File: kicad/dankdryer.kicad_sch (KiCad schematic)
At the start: 25 parts, among them J1 Barreljack, J4 heater, J5 Screw_Terminal_01x04, J7 5kg load cell, J8 motor, J9 Conn_01x04, U2 TPS62162DSG, U3 HT7550, U6 ESP32-C6-MINI-1U-H4

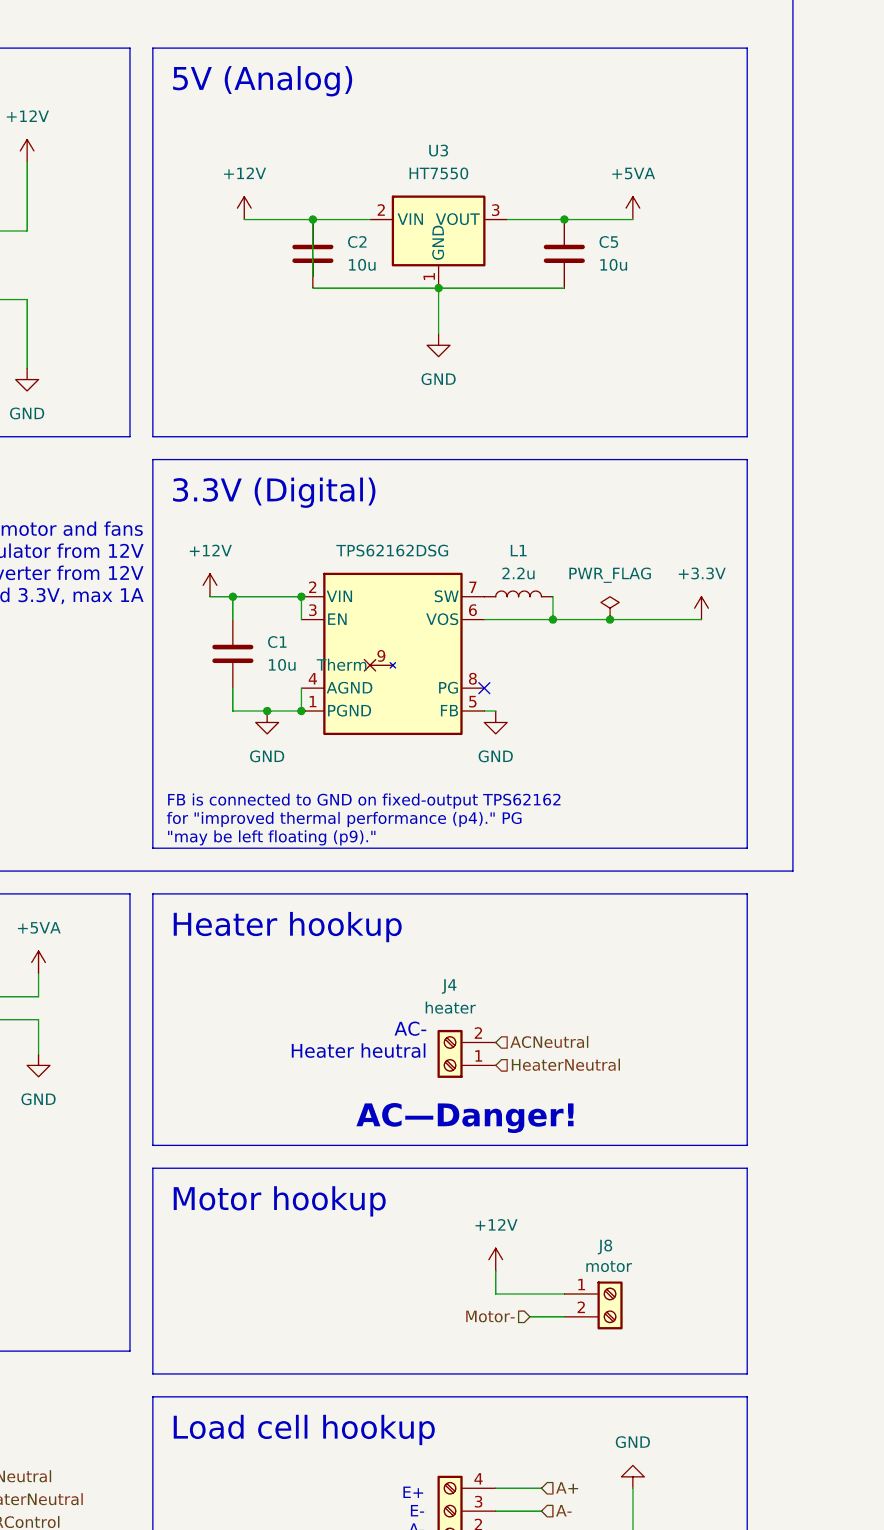
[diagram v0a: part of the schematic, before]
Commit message: kicad: note about AVDD on NAU7802
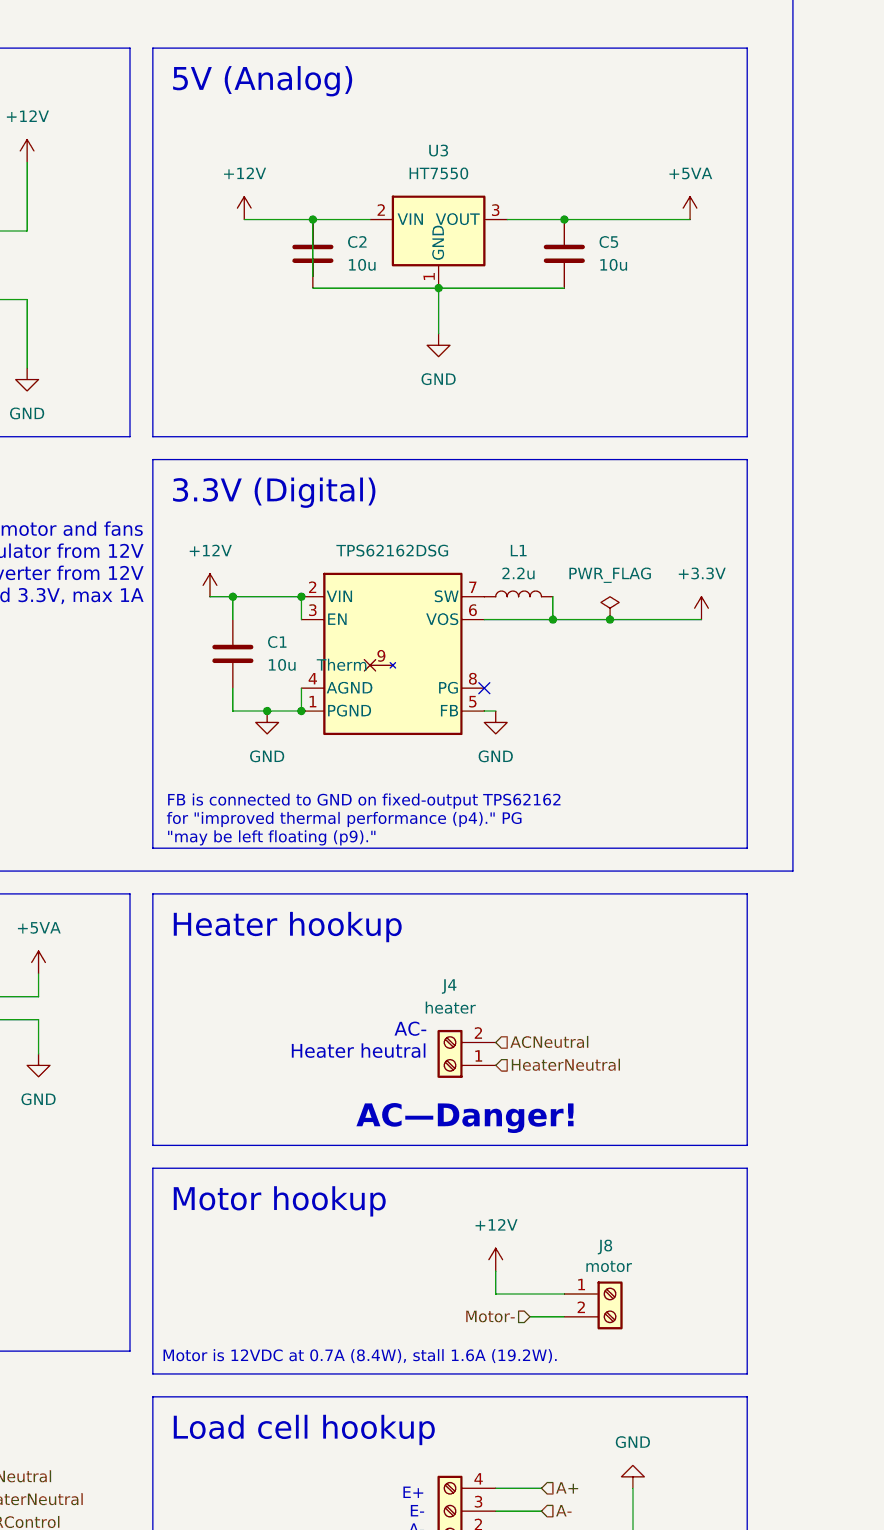
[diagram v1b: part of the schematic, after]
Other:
- note added: "Motor is 12VDC at 0.7A (8.4W), stall 1.6A (19.2W)."
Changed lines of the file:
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@@
 	(wire
 		(pts
-			(xy 134.62 41.91) (xy 142.24 41.91)
+			(xy 134.62 41.91) (xy 148.59 41.91)
 		)
 		(stroke
@@
 		(exclude_from_sim no)
 		(at 21.336 164.084 0)
+		(effects
+			(font
+				(size 1.27 1.27)
+			)
+			(justify left)
+		)
+	)
+	(text "Motor is 12VDC at 0.7A (8.4W), stall 1.6A (19.2W)."
+		(exclude_from_sim no)
+		(at 89.916 168.402 0)
 		(effects
 			(font
@@
 	(symbol
 		(lib_id "power:+5VA")
-		(at 142.24 41.91 0)
+		(at 148.59 41.91 0)
 		(unit 1)
 		(exclude_from_sim no)
@@
 		(fields_autoplaced yes)
 		(property "Reference" "#PWR015"
-			(at 142.24 45.72 0)
+			(at 148.59 45.72 0)
 			(effects
 				(font
@@
 		)
 		(property "Value" "+5VA"
-			(at 142.24 36.83 0)
+			(at 148.59 36.83 0)
 			(effects
 				(font
@@
 		)
 		(property "Footprint" ""
-			(at 142.24 41.91 0)
+			(at 148.59 41.91 0)
 			(effects
 				(font
@@
 		)
 		(property "Datasheet" ""
-			(at 142.24 41.91 0)
+			(at 148.59 41.91 0)
 			(effects
 				(font
@@
 		)
 		(property "Description" "Power symbol creates a global label with name \"+5VA\""
-			(at 142.24 41.91 0)
+			(at 148.59 41.91 0)
 			(effects
 				(font

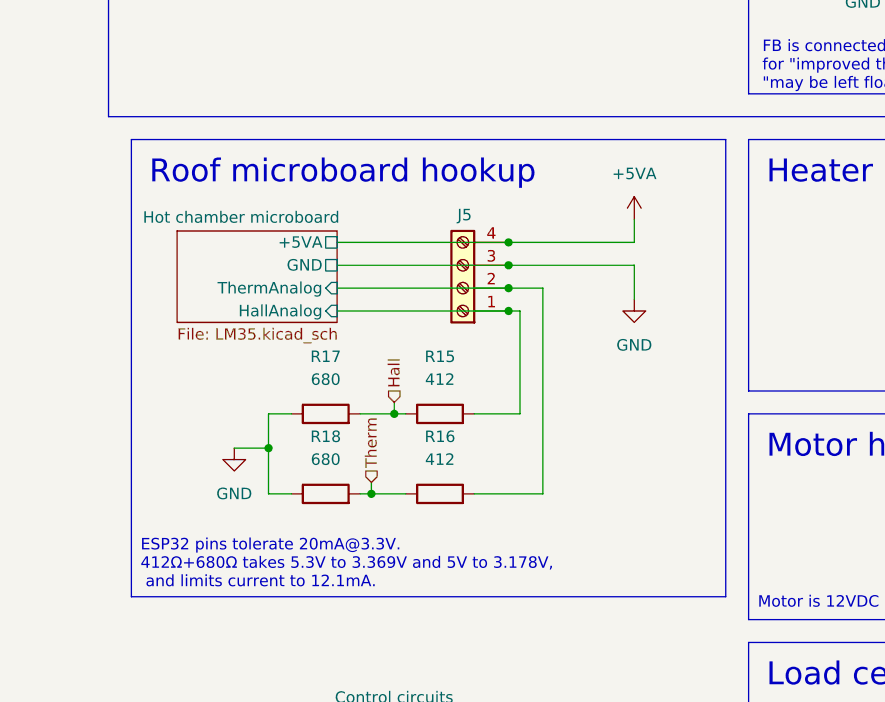
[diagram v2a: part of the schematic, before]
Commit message: take 3.3V to microboard rather than dividing 5V on return from hall sensor
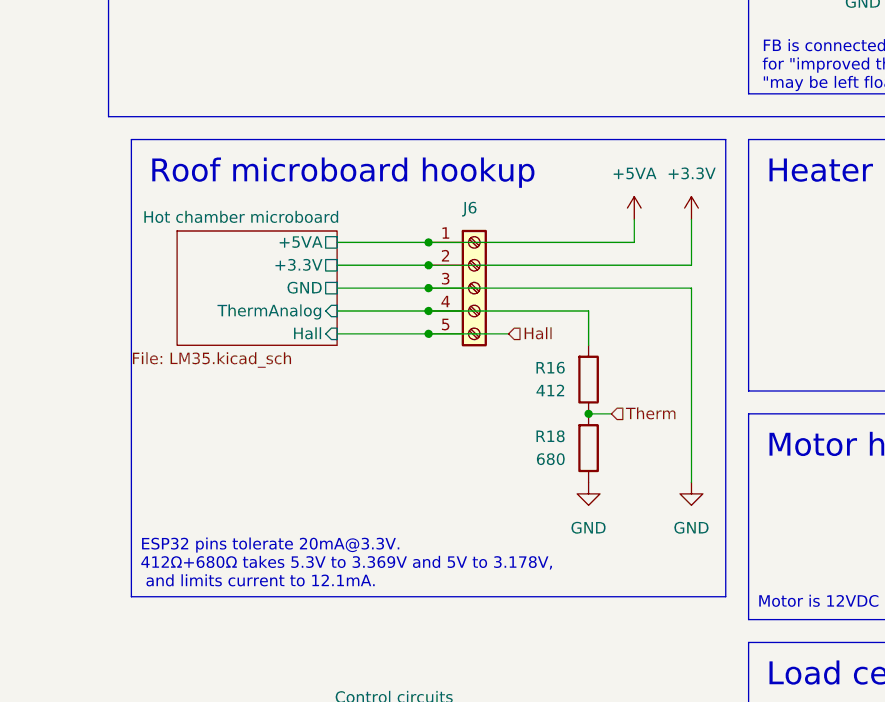
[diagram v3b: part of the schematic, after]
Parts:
- removed J5: Screw_Terminal_01x04, dank:TerminalBlock_bornier-4_P5.08mm, symbol Connector:Screw_Terminal_01x04
- removed R15: 412, PCM_Resistor_SMD_AKL:R_0805_2012Metric_Pad1.15x1.40mm_HandSolder, symbol Device:R
- removed R17: 680, PCM_Resistor_SMD_AKL:R_0805_2012Metric_Pad1.15x1.40mm_HandSolder, symbol Device:R
- added J6: Screw_Terminal_01x05, dank:TerminalBlock_bornier-5_P5.08mm, symbol Connector:Screw_Terminal_01x05
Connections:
- net +3.3V: now also J6.2 (Pin_2)
- net +5VA: now also J6.1 (Pin_1)
- net GND: now also J6.3 (Pin_3)
- net Hall: now also J6.5 (Pin_5)
- net Hot chamber microboard/ThermAnalog: now also J6.4 (Pin_4)
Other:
- sheet Hot chamber microboard ports: added +3.3V, Hall; removed HallAnalog
- moved on the sheet: R16, R18

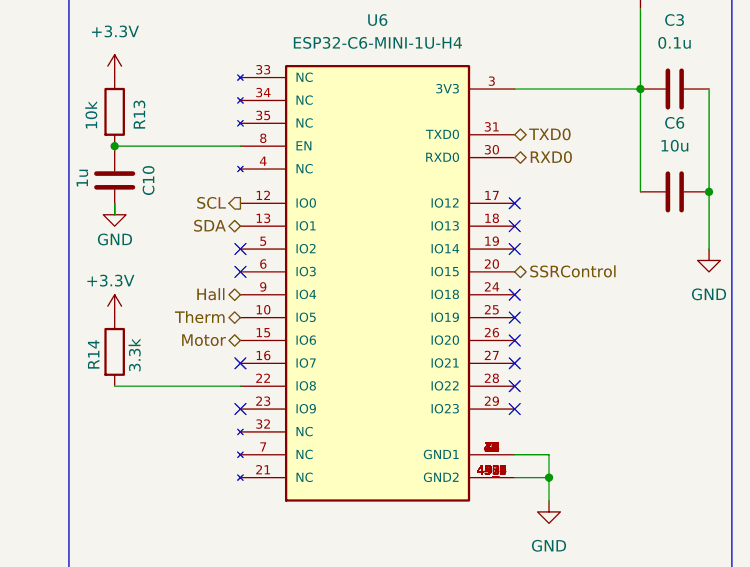
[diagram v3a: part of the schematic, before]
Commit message: get off the strapping pins. hardware version 1.0
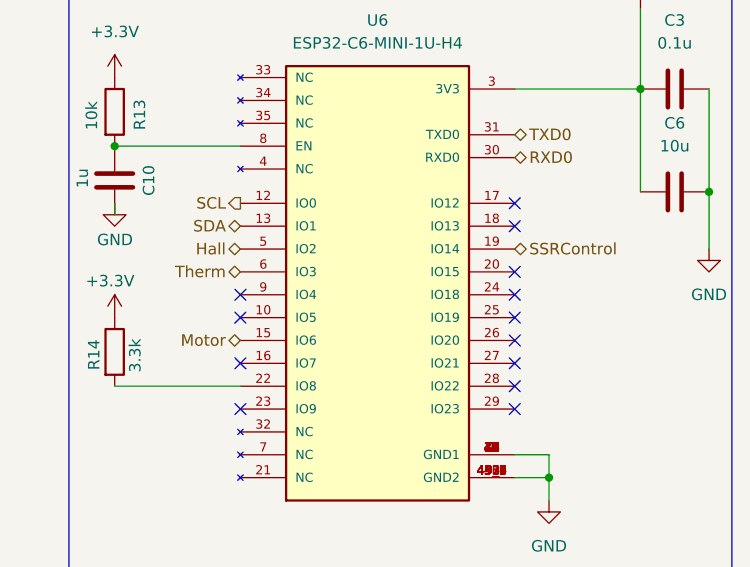
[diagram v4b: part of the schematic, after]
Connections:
- net Hall: now also U6.5 (IO2); no longer U6.9 (IO4)
- net SSRControl: now also U6.19 (IO14); no longer U6.20 (IO15)
- net Therm: now also U6.6 (IO3); no longer U6.10 (IO5)
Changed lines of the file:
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@@
 	(title_block
 		(title "Dankdryer")
-		(date "2024-12-26")
-		(rev "0.99")
+		(date "2024-12-31")
+		(rev "1.0")
 		(company "Dirty South Supercomputing")
 		(comment 1 "nick black")
@@
 	)
 	(no_connect
+		(at 189.23 69.85)
+	)
+	(no_connect
 		(at 219.71 57.15)
 	)
 	(no_connect
-		(at 189.23 62.23)
-	)
-	(no_connect
 		(at 219.71 77.47)
 	)
@@
 	)
 	(no_connect
-		(at 189.23 64.77)
-	)
-	(no_connect
 		(at 125.73 93.98)
 	)
 	(no_connect
-		(at 219.71 62.23)
+		(at 189.23 67.31)
 	)
 	(no_connect
 		(at 44.45 45.72)
+	)
+	(no_connect
+		(at 219.71 64.77)
 	)
 	(no_connect
@@
 	(hierarchical_label "Hall"
 		(shape bidirectional)
-		(at 189.23 67.31 180)
+		(at 189.23 62.23 180)
 		(fields_autoplaced yes)
 		(effects
@@
 			)
 			(justify right)
-		)
-	)
-	(hierarchical_label "SSRControl"
-		(shape bidirectional)
-		(at 219.71 64.77 0)
-		(fields_autoplaced yes)
-		(effects
-			(font
-				(size 1.27 1.27)
-			)
-			(justify left)
 		)
 	)
@@
 		)
 	)
-	(hierarchical_label "Therm"
-		(shape bidirectional)
-		(at 189.23 69.85 180)
-		(fields_autoplaced yes)
-		(effects
-			(font
-				(size 1.27 1.27)
-			)
-			(justify right)
-		)
-	)
 	(hierarchical_label "HeaterNeutral"
 		(shape input)
@@
 		)
 	)
+	(hierarchical_label "Therm"
+		(shape bidirectional)
+		(at 189.23 64.77 180)
+		(fields_autoplaced yes)
+		(effects
+			(font
+				(size 1.27 1.27)
+			)
+			(justify right)
+		)
+	)
+	(hierarchical_label "SSRControl"
+		(shape bidirectional)
+		(at 219.71 62.23 0)
+		(fields_autoplaced yes)
+		(effects
+			(font
+				(size 1.27 1.27)
+			)
+			(justify left)
+		)
+	)

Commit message: tighten up pcb a bit more
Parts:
- U6: value ESP32-C6-MINI-1U-H4 -> ESP32-C6-MINI-1U
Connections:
- net +12V: now also J8.2 (Pin_2); no longer J8.1 (Pin_1)
- net +3.3V: now also J6.4 (Pin_4); no longer J6.2 (Pin_2)
- net +5VA: now also J6.5 (Pin_5); no longer J6.1 (Pin_1)
- net Hall: now also J6.1 (Pin_1); no longer J6.5 (Pin_5)
- net Hot chamber microboard/ThermAnalog: now also J6.2 (Pin_2); no longer J6.4 (Pin_4)
- net Motor-: now also J8.1 (Pin_1); no longer J8.2 (Pin_2)
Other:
- note added: "ESP32-C6-MINI-1U: unicore 160MHz RISC-V. 4MB QSPI flash, 40–105C. GPIOs 0-6 are connected to 12-bit ADC. GPIOs 4, 5, 8, 9, and 15 are strapping pins. GPIOs 12 and 13 are used for JTAG. GPIOs 24-30 are used for QSPI flash. Module has a U.FL antenna connector."
- note removed: "Unicore 160MHz RISC-V. 4MB QSPI flash, 40–105C. GPIOs 0-6 are connected to 12-bit ADC. GPIOs 4, 5, 8, 9, and 15 are strapping pins. GPIOs 12 and 13 are used for JTAG. GPIOs 24-30 are used for QSPI flash. Module has a U.FL antenna connector."
- moved on the sheet: J6, J8
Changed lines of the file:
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@@
 	(title_block
 		(title "Dankdryer")
-		(date "2024-12-31")
-		(rev "1.0")
+		(date "2025-01-02")
+		(rev "1.0.1")
 		(company "Dirty South Supercomputing")
 		(comment 1 "nick black")
@@
 	)
 	(junction
+		(at 58.42 138.43)
+		(diameter 0)
+		(color 0 0 0 0)
+	)
+	(junction
 		(at 106.68 41.91)
 		(diameter 0)
@@
 	)
 	(junction
-		(at 53.34 138.43)
+		(at 58.42 135.89)
 		(diameter 0)
 		(color 0 0 0 0)
 	)
 	(junction
-		(at 53.34 128.27)
+		(at 97.79 83.82)
 		(diameter 0)
 		(color 0 0 0 0)
 	)
 	(junction
-		(at 97.79 83.82)
+		(at 58.42 128.27)
 		(diameter 0)
 		(color 0 0 0 0)
 	)
 	(junction
-		(at 53.34 133.35)
+		(at 58.42 130.81)
 		(diameter 0)
 		(color 0 0 0 0)
@@
 	)
 	(junction
-		(at 53.34 130.81)
-		(diameter 0)
-		(color 0 0 0 0)
-	)
-	(junction
-		(at 53.34 135.89)
+		(at 58.42 133.35)
 		(diameter 0)
 		(color 0 0 0 0)
@@
 	(wire
 		(pts
-			(xy 127 161.29) (xy 134.62 161.29)
+			(xy 58.42 133.35) (xy 82.55 133.35)
 		)
 		(stroke
@@
 	(wire
 		(pts
-			(xy 43.18 130.81) (xy 53.34 130.81)
-		)
-		(stroke
-			(width 0)
-			(type default)
-		)
-	)
-	(wire
-		(pts
-			(xy 53.34 135.89) (xy 71.12 135.89)
+			(xy 43.18 130.81) (xy 58.42 130.81)
 		)
 		(stroke
@@
 	(wire
 		(pts
-			(xy 43.18 133.35) (xy 53.34 133.35)
+			(xy 43.18 133.35) (xy 58.42 133.35)
 		)
 		(stroke
@@
 	(wire
 		(pts
-			(xy 53.34 138.43) (xy 62.23 138.43)
+			(xy 58.42 138.43) (xy 59.69 138.43)
 		)
 		(stroke
@@
 	(wire
 		(pts
+			(xy 58.42 130.81) (xy 82.55 130.81)
+		)
+		(stroke
+			(width 0)
+			(type default)
+		)
+	)
+	(wire
+		(pts
 			(xy 241.3 44.45) (xy 241.3 55.88)
 		)
@@
 	(wire
 		(pts
+			(xy 127 157.48) (xy 127 154.94)
+		)
+		(stroke
+			(width 0)
+			(type default)
+		)
+	)
+	(wire
+		(pts
 			(xy 191.77 132.08) (xy 196.85 132.08)
 		)
@@
 	(wire
 		(pts
-			(xy 82.55 133.35) (xy 53.34 133.35)
+			(xy 134.62 41.91) (xy 148.59 41.91)
 		)
 		(stroke
@@
 	(wire
 		(pts
-			(xy 134.62 41.91) (xy 148.59 41.91)
+			(xy 52.07 43.18) (xy 67.31 43.18)
 		)
 		(stroke
@@
 	(wire
 		(pts
-			(xy 52.07 43.18) (xy 67.31 43.18)
+			(xy 105.41 86.36) (xy 105.41 83.82)
 		)
 		(stroke
@@
 	(wire
 		(pts
-			(xy 105.41 86.36) (xy 105.41 83.82)
+			(xy 97.79 83.82) (xy 97.79 86.36)
 		)
 		(stroke
@@
 	(wire
 		(pts
-			(xy 97.79 83.82) (xy 97.79 86.36)
+			(xy 43.18 128.27) (xy 58.42 128.27)
 		)
 		(stroke
@@
 	(wire
 		(pts
-			(xy 43.18 128.27) (xy 53.34 128.27)
+			(xy 175.26 77.47) (xy 189.23 77.47)
 		)
 		(stroke
@@
 	(wire
 		(pts
-			(xy 175.26 77.47) (xy 189.23 77.47)
+			(xy 58.42 135.89) (xy 71.12 135.89)
 		)
 		(stroke
@@
 	(wire
 		(pts
-			(xy 43.18 138.43) (xy 53.34 138.43)
+			(xy 43.18 138.43) (xy 58.42 138.43)
 		)
 		(stroke
@@
 	(wire
 		(pts
-			(xy 82.55 130.81) (xy 53.34 130.81)
-		)
-		(stroke
-			(width 0)
-			(type default)
-		)
-	)
-	(wire
-		(pts
-			(xy 53.34 128.27) (xy 76.2 128.27)
-		)
-		(stroke
-			(width 0)
-			(type default)
-		)
-	)
-	(wire
-		(pts
 			(xy 132.08 185.42) (xy 127 185.42)
 		)
@@
 	(wire
 		(pts
-			(xy 127 161.29) (xy 127 158.75)
-		)
-		(stroke
-			(width 0)
-			(type default)
-		)
-	)
-	(wire
-		(pts
 			(xy 67.31 189.23) (xy 63.5 189.23)
 		)
@@
 	(wire
 		(pts
+			(xy 120.65 160.02) (xy 129.54 160.02)
+		)
+		(stroke
+			(width 0)
+			(type default)
+		)
+	)
+	(wire
+		(pts
 			(xy 34.29 181.61) (xy 36.83 181.61)
 		)
@@
 	(wire
 		(pts
-			(xy 67.31 186.69) (xy 63.5 186.69)
+			(xy 120.65 157.48) (xy 127 157.48)
 		)
 		(stroke
@@
 	(wire
 		(pts
-			(xy 130.81 163.83) (xy 134.62 163.83)
+			(xy 67.31 186.69) (xy 63.5 186.69)
 		)
 		(stroke
@@
 	(wire
 		(pts
-			(xy 43.18 135.89) (xy 53.34 135.89)
+			(xy 43.18 135.89) (xy 58.42 135.89)
+		)
+		(stroke
+			(width 0)
+			(type default)
+		)
+	)
+	(wire
+		(pts
+			(xy 58.42 128.27) (xy 76.2 128.27)
 		)
 		(stroke
@@
 		)
 	)
-	(text "Unicore 160MHz RISC-V. 4MB QSPI flash, 40–105C.\nGPIOs 0-6 are connected to 12-bit ADC.\nGPIOs 4, 5, 8, 9, and 15 are strapping pins.\nGPIOs 12 and 13 are used for JTAG.\nGPIOs 24-30 are used for QSPI flash.\nModule has a U.FL antenna connector."
+	(text "ESP32-C6-MINI-1U: unicore 160MHz RISC-V. 4MB QSPI flash, 40–105C.\nGPIOs 0-6 are connected to 12-bit ADC.\nGPIOs 4, 5, 8, 9, and 15 are strapping pins.\nGPIOs 12 and 13 are used for JTAG.\nGPIOs 24-30 are used for QSPI flash.\nModule has a U.FL antenna connector."
 		(exclude_from_sim no)
 		(at 171.704 108.204 0)
@@
 	(hierarchical_label "Hall"
 		(shape input)
-		(at 62.23 138.43 0)
+		(at 59.69 138.43 0)
 		(fields_autoplaced yes)
 		(effects
@@
 	(hierarchical_label "Motor-"
 		(shape input)
-		(at 130.81 163.83 180)
+		(at 129.54 160.02 0)
 		(fields_autoplaced yes)
 		(effects
@@
 				(size 1.27 1.27)
 			)
-			(justify right)
+			(justify left)
 		)
 	)
@@
 	(symbol
 		(lib_id "Connector:Screw_Terminal_01x02")
-		(at 139.7 161.29 0)
+		(at 115.57 160.02 180)
 		(unit 1)
 		(exclude_from_sim no)
@@
 		(dnp no)
 		(property "Reference" "J8"
-			(at 138.43 155.956 0)
+			(at 116.84 165.354 0)
 			(effects
 				(font
@@
 		)
 		(property "Value" "motor"
-			(at 136.906 158.242 0)
+			(at 118.364 163.068 0)
 			(effects
 				(font
@@
 		)
 		(property "Footprint" "dank:TerminalBlock_bornier-2_P5.08mm"
-			(at 139.7 161.29 0)
+			(at 115.57 160.02 0)
 			(effects
 				(font
@@
 		)
 		(property "Datasheet" "~"
-			(at 139.7 161.29 0)
+			(at 115.57 160.02 0)
 			(effects
 				(font
@@
 		)
 		(property "Description" "Generic screw terminal, single row, 01x02, script generated (kicad-library-utils/schlib/autogen/connector/)"
-			(at 139.7 161.29 0)
+			(at 115.57 160.02 0)
 			(effects
 				(font
@@
 	(symbol
 		(lib_id "power:+12V")
-		(at 127 158.75 0)
+		(at 127 154.94 0)
 		(unit 1)
 		(exclude_from_sim no)
@@
 		(on_board yes)
 		(dnp no)
-		(fields_autoplaced yes)
 		(property "Reference" "#PWR033"
-			(at 127 162.56 0)
+			(at 127 158.75 0)
 			(effects
 				(font
@@
 		)
 		(property "Value" "+12V"
-			(at 127 153.67 0)
+			(at 127 149.86 0)
 			(effects
 				(font
@@
 		)
 		(property "Footprint" ""
-			(at 127 158.75 0)
+			(at 127 154.94 0)
 			(effects
 				(font
@@
 		)
 		(property "Datasheet" ""
-			(at 127 158.75 0)
+			(at 127 154.94 0)
 			(effects
 				(font
@@
 		)
 		(property "Description" "Power symbol creates a global label with name \"+12V\""
-			(at 127 158.75 0)
+			(at 127 154.94 0)
 			(effects
 				(font
@@
 	(symbol
 		(lib_id "Connector:Screw_Terminal_01x05")
-		(at 58.42 133.35 0)
+		(at 53.34 133.35 180)
 		(unit 1)
 		(exclude_from_sim no)
@@
 		(dnp no)
 		(property "Reference" "J6"
-			(at 57.15 124.46 0)
+			(at 54.61 142.24 0)
 			(effects
 				(font
@@
 		)
 		(property "Value" "Screw_Terminal_01x05"
-			(at 41.148 149.098 0)
+			(at 70.612 117.602 0)
 			(effects
 				(font
@@
 		)
 		(property "Footprint" "dank:TerminalBlock_bornier-5_P5.08mm"
-			(at 58.42 133.35 0)
+			(at 53.34 133.35 0)
 			(effects
 				(font
@@
 		)
 		(property "Datasheet" "~"
-			(at 58.42 133.35 0)
+			(at 53.34 133.35 0)
 			(effects
 				(font
@@
 		)
 		(property "Description" "Generic screw terminal, single row, 01x05, script generated (kicad-library-utils/schlib/autogen/connector/)"
-			(at 58.42 133.35 0)
+			(at 53.34 133.35 0)
 			(effects
 				(font
@@
 			)
 		)
-		(property "Value" "ESP32-C6-MINI-1U-H4"
+		(property "Value" "ESP32-C6-MINI-1U"
 			(at 204.47 39.37 0)
 			(effects

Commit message: replace NAU7802SGI with NAU7802KGI i accidentally bought
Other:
- company: Dirty South Supercomputing -> dirty south supercomputing
- title: Dankdryer -> dankdryer
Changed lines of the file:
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@@
 	(paper "USLetter")
 	(title_block
-		(title "Dankdryer")
-		(date "2025-01-02")
-		(rev "1.0.1")
-		(company "Dirty South Supercomputing")
+		(title "dankdryer")
+		(date "2025-01-05")
+		(rev "1.1.0")
+		(company "dirty south supercomputing")
 		(comment 1 "nick black")
 	)
